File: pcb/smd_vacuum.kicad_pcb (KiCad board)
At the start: 2 copper layers, 71 x 72.4 mm, 29 parts, among them J1 PWR, M1 Motor_DC, Q1 Q_PMOS_GDS, Q2 Q_NMOS_GDS, Q3 Q_NMOS_GDS, SW1 SW_SPST, U1 NE555P, U2 EL817

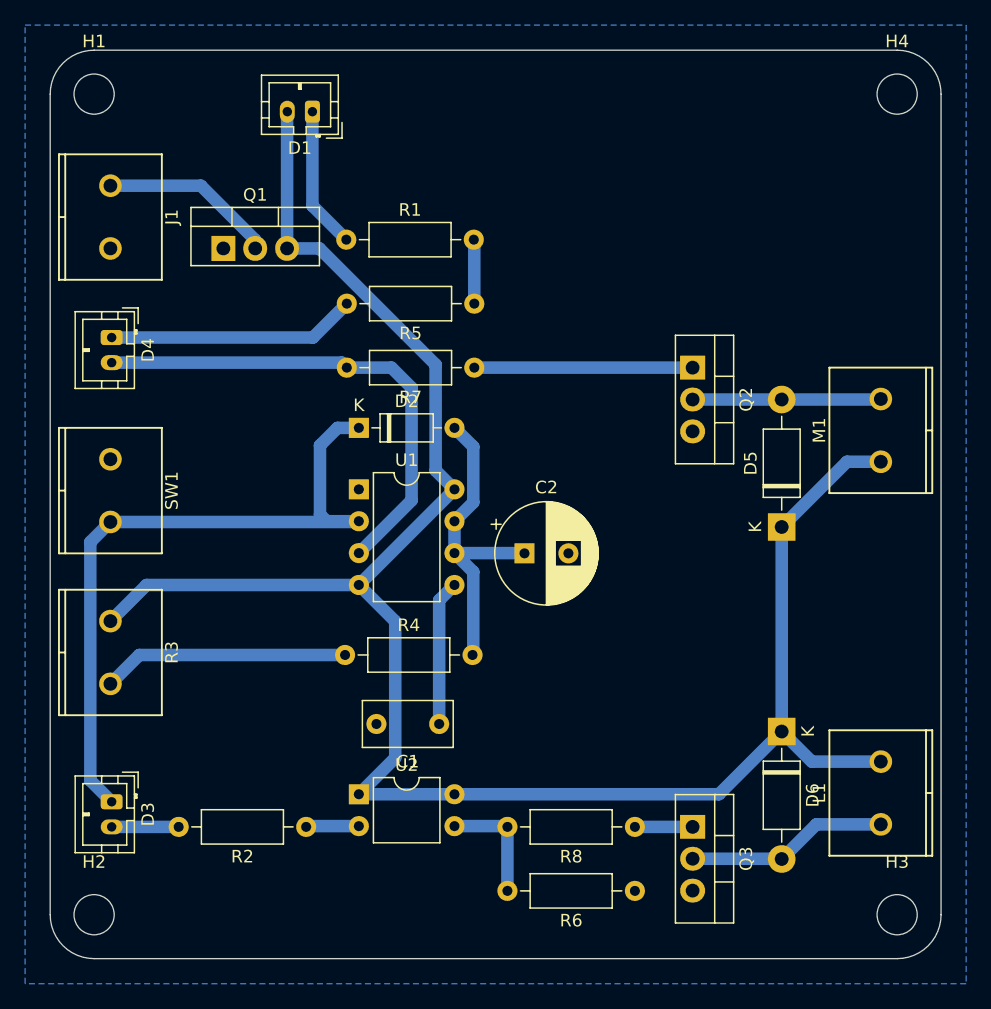
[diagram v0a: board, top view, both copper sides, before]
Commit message: layout pcb with reset circuitry
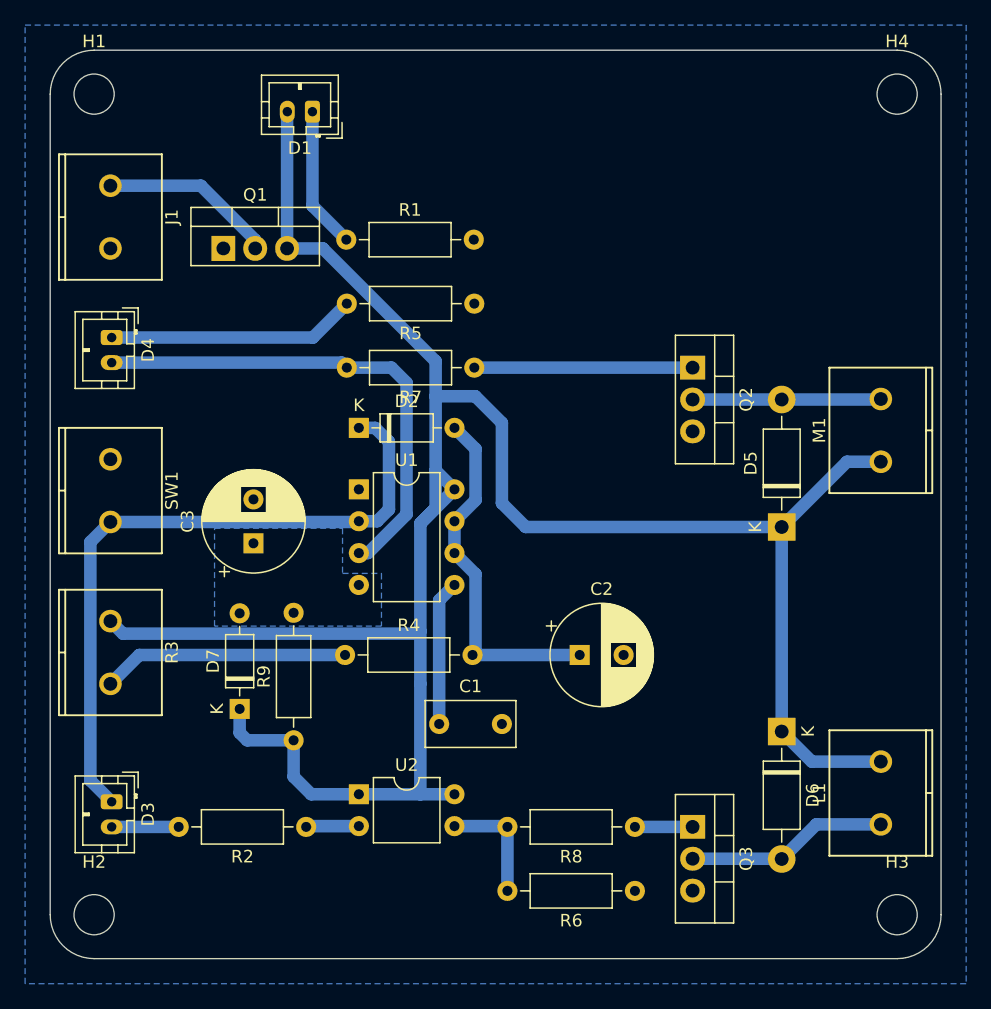
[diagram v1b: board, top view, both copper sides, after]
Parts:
- added C3: 100u, Capacitor_THT:CP_Radial_D8.0mm_P3.50mm, F.Cu at (121.9, 82.7)
- added D7: 1N4148, Diode_THT:D_DO-35_SOD27_P7.62mm_Horizontal, F.Cu at (120.8, 95.9)
- added R9: 1k, Resistor_THT:R_Axial_DIN0207_L6.3mm_D2.5mm_P10.16mm_Horizontal, F.Cu at (125.1, 98.4)
- Q1: value Q_PMOS_GDS -> IRF5305
- moved C2 9.22 mm to (147.9, 91.6)
- turned C1 to 0 degrees
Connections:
- U1 pad 4: +12V -> Net-(C3-Pad1)
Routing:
- net +12V: track 159.0 -> 186.3 mm
- net GND: track 5.12 -> 0.06 mm
- net Net-(C2-Pad1): track 25.6 -> 28.8 mm
- net Net-(D2-Pad1): track 56.0 -> 54.5 mm
- added copper zone on B.Cu, net Net-(C3-Pad1)
